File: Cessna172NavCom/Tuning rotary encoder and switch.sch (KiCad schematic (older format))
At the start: 7 parts, among them J3 EN11-HSM1BF20

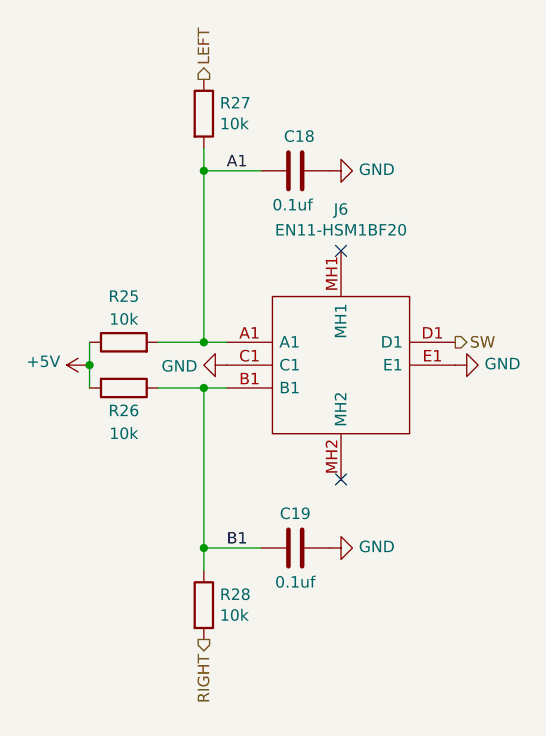
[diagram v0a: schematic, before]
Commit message: Smaller components and output for JLC
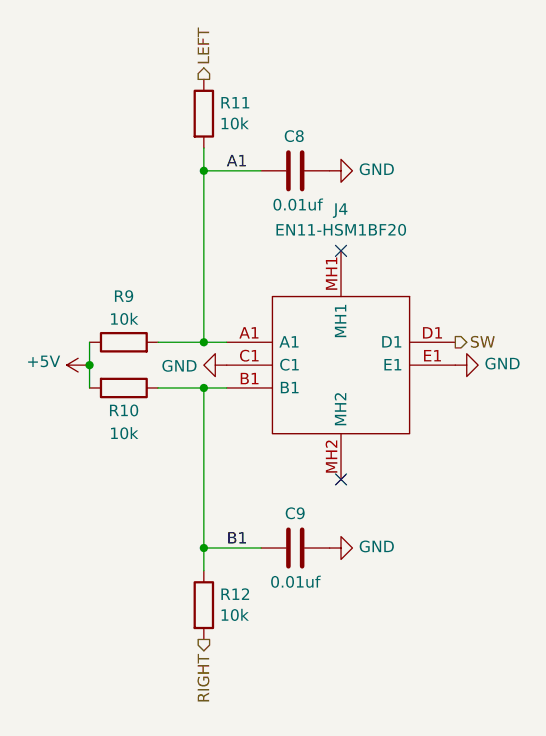
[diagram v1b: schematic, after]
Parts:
- C6, C7: value 0.1uf -> 0.01uf; footprint Capacitor_SMD:C_0805_2012Metric_Pad1.15x1.40mm_HandSolder -> Capacitor_SMD:C_0603_1608Metric; LCSC (none) -> C57112; LCSC Part # (none) -> C57112
- R5, R6, R7, R8: footprint Resistor_SMD:R_0805_2012Metric_Pad1.15x1.40mm_HandSolder -> Resistor_SMD:R_0603_1608Metric; LCSC (none) -> C25804; LCSC Part # (none) -> C25804
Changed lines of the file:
@@
 $Descr A4 11693 8268
 encoding utf-8
-Sheet 13 13
+Sheet 6 13
 Title ""
 Date ""
@@
 AR Path="/5F71BCEB/5F5D9328" Ref="R25"  Part="1"
 AR Path="/5F71BCF7/5F5D9328" Ref="R29"  Part="1"
-F 0 "R25" V 5450 3850 50  0000 C CNN
+F 0 "R9" V 5450 3850 50  0000 C CNN
 F 1 "10k" V 5350 3850 50  0000 C CNN
-F 2 "Resistor_SMD:R_0805_2012Metric_Pad1.15x1.40mm_HandSolder" V 5180 3850 50  0001 C CNN
+F 2 "Resistor_SMD:R_0603_1608Metric" V 5180 3850 50  0001 C CNN
 F 3 "~" H 5250 3850 50  0001 C CNN
+F 4 "C25804" H 5250 3850 50  0001 C CNN "LCSC Part #"
+F 5 "C25804" H 5250 3850 50  0001 C CNN "LCSC"
 	1    5250 3850
 	0    -1   -1   0
@@
 AR Path="/5F71BCEB/5F5D932E" Ref="R26"  Part="1"
 AR Path="/5F71BCF7/5F5D932E" Ref="R30"  Part="1"
-F 0 "R26" V 5350 4050 50  0000 C CNN
+F 0 "R10" V 5350 4050 50  0000 C CNN
 F 1 "10k" V 5450 4050 50  0000 C CNN
-F 2 "Resistor_SMD:R_0805_2012Metric_Pad1.15x1.40mm_HandSolder" V 5180 4050 50  0001 C CNN
+F 2 "Resistor_SMD:R_0603_1608Metric" V 5180 4050 50  0001 C CNN
 F 3 "~" H 5250 4050 50  0001 C CNN
+F 4 "C25804" H 5250 4050 50  0001 C CNN "LCSC Part #"
+F 5 "C25804" H 5250 4050 50  0001 C CNN "LCSC"
 	1    5250 4050
 	0    1    1    0
@@
 AR Path="/5F71BCEB/5F5D9337" Ref="C19"  Part="1"
 AR Path="/5F71BCF7/5F5D9337" Ref="C21"  Part="1"
-F 0 "C19" V 6150 4750 50  0000 C CNN
-F 1 "0.1uf" V 5850 4750 50  0000 C CNN
-F 2 "Capacitor_SMD:C_0805_2012Metric_Pad1.15x1.40mm_HandSolder" H 6038 4600 50  0001 C CNN
+F 0 "C9" V 6150 4750 50  0000 C CNN
+F 1 "0.01uf" V 5850 4750 50  0000 C CNN
+F 2 "Capacitor_SMD:C_0603_1608Metric" H 6038 4600 50  0001 C CNN
 F 3 "~" H 6000 4750 50  0001 C CNN
+F 4 "C57112" H 6000 4750 50  0001 C CNN "LCSC Part #"
+F 5 "C57112" H 6000 4750 50  0001 C CNN "LCSC"
 	1    6000 4750
 	0    -1   -1   0
@@
 AR Path="/5F71BCEB/5F5D933D" Ref="C18"  Part="1"
 AR Path="/5F71BCF7/5F5D933D" Ref="C20"  Part="1"
-F 0 "C18" V 5850 3050 50  0000 L CNN
-F 1 "0.1uf" V 6150 3000 50  0000 L CNN
-F 2 "Capacitor_SMD:C_0805_2012Metric_Pad1.15x1.40mm_HandSolder" H 6038 2950 50  0001 C CNN
+F 0 "C8" V 5850 3050 50  0000 L CNN
+F 1 "0.01uf" V 6150 3000 50  0000 L CNN
+F 2 "Capacitor_SMD:C_0603_1608Metric" H 6038 2950 50  0001 C CNN
 F 3 "~" H 6000 3100 50  0001 C CNN
+F 4 "C57112" H 6000 3100 50  0001 C CNN "LCSC Part #"
+F 5 "C57112" H 6000 3100 50  0001 C CNN "LCSC"
 	1    6000 3100
 	0    1    1    0
@@
 AR Path="/5F71BCEB/5F5D934C" Ref="R28"  Part="1"
 AR Path="/5F71BCF7/5F5D934C" Ref="R32"  Part="1"
-F 0 "R28" H 5670 5046 50  0000 L CNN
+F 0 "R12" H 5670 5046 50  0000 L CNN
 F 1 "10k" H 5670 4955 50  0000 L CNN
-F 2 "Resistor_SMD:R_0805_2012Metric_Pad1.15x1.40mm_HandSolder" V 5530 5000 50  0001 C CNN
+F 2 "Resistor_SMD:R_0603_1608Metric" V 5530 5000 50  0001 C CNN
 F 3 "~" H 5600 5000 50  0001 C CNN
+F 4 "C25804" H 5600 5000 50  0001 C CNN "LCSC Part #"
+F 5 "C25804" H 5600 5000 50  0001 C CNN "LCSC"
 	1    5600 5000
 	1    0    0    -1
@@
 AR Path="/5F71BCEB/5F5D935D" Ref="R27"  Part="1"
 AR Path="/5F71BCF7/5F5D935D" Ref="R31"  Part="1"
-F 0 "R27" H 5670 2896 50  0000 L CNN
+F 0 "R11" H 5670 2896 50  0000 L CNN
 F 1 "10k" H 5670 2805 50  0000 L CNN
-F 2 "Resistor_SMD:R_0805_2012Metric_Pad1.15x1.40mm_HandSolder" V 5530 2850 50  0001 C CNN
+F 2 "Resistor_SMD:R_0603_1608Metric" V 5530 2850 50  0001 C CNN
 F 3 "~" H 5600 2850 50  0001 C CNN
+F 4 "C25804" H 5600 2850 50  0001 C CNN "LCSC Part #"
+F 5 "C25804" H 5600 2850 50  0001 C CNN "LCSC"
 	1    5600 2850
 	1    0    0    -1
@@
 AR Path="/5F71BCEB/5F66C873" Ref="J6"  Part="1"
 AR Path="/5F71BCF7/5F66C873" Ref="J7"  Part="1"
-F 0 "J6" V 6019 3450 50  0000 C CNN
+F 0 "J4" V 6019 3450 50  0000 C CNN
 F 1 "EN11-HSM1BF20" V 6110 3450 50  0000 C CNN
 F 2 "SamacSys_Parts:EN11HSM1BF20" H 7050 3750 50  0001 L CNN
